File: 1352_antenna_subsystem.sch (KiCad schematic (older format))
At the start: 12 parts

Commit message: did more work on the schematic
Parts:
- AE1: renamed from AE; footprint (none) -> Connector_Coaxial:U.FL_Hirose_U.FL-R-SMT-1_Vertical
- C1, C2: renamed from C?; value C -> 1.1pF; footprint (none) -> Capacitor_SMD:C_0201_0603Metric_Pad0.64x0.40mm_HandSolder
- C3: renamed from C?; value C -> 12pF; footprint (none) -> Capacitor_SMD:C_0201_0603Metric_Pad0.64x0.40mm_HandSolder
- C4: renamed from C?; value C -> 1pF; footprint (none) -> Capacitor_SMD:C_0201_0603Metric_Pad0.64x0.40mm_HandSolder
- C5: renamed from C?; value C -> 47pF; footprint (none) -> Capacitor_SMD:C_0201_0603Metric_Pad0.64x0.40mm_HandSolder
- L1: renamed from L?; value L -> 15nH; footprint (none) -> Inductor_SMD:L_0201_0603Metric_Pad0.64x0.40mm_HandSolder
- L2, L3: renamed from L?; value L -> 2.4nH; footprint (none) -> Inductor_SMD:L_0201_0603Metric_Pad0.64x0.40mm_HandSolder
- L4: renamed from L?; value L -> 1nH; footprint (none) -> Inductor_SMD:L_0201_0603Metric_Pad0.64x0.40mm_HandSolder
- L5: renamed from L?; value L -> 3.3nH; footprint (none) -> Inductor_SMD:L_0201_0603Metric_Pad0.64x0.40mm_HandSolder
- gave numbers to parts that had none: 1
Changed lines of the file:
@@
 $EndDescr
 $Comp
-L power:GND #PWR?
+L power:GND #PWR0101
 U 1 1 603957EF
 P 3800 3950
-F 0 "#PWR?" H 3800 3700 50  0001 C CNN
+F 0 "#PWR0101" H 3800 3700 50  0001 C CNN
 F 1 "GND" H 3805 3777 50  0000 C CNN
 F 2 "" H 3800 3950 50  0001 C CNN
@@
 $EndComp
 $Comp
-L power:GND #PWR?
+L power:GND #PWR0102
 U 1 1 603965C6
 P 2250 4100
-F 0 "#PWR?" H 2250 3850 50  0001 C CNN
+F 0 "#PWR0102" H 2250 3850 50  0001 C CNN
 F 1 "GND" H 2255 3927 50  0000 C CNN
 F 2 "" H 2250 4100 50  0001 C CNN
@@
 $EndComp
 $Comp
-L Device:C C?
+L Device:C C1
 U 1 1 6039A1F9
 P 2250 3800
-F 0 "C?" H 2365 3846 50  0000 L CNN
-F 1 "C" H 2365 3755 50  0000 L CNN
-F 2 "" H 2288 3650 50  0001 C CNN
+F 0 "C1" H 2365 3846 50  0000 L CNN
+F 1 "1.1pF" H 2365 3755 50  0000 L CNN
+F 2 "Capacitor_SMD:C_0201_0603Metric_Pad0.64x0.40mm_HandSolder" H 2288 3650 50  0001 C CNN
 F 3 "~" H 2250 3800 50  0001 C CNN
 	1    2250 3800
@@
 $EndComp
 $Comp
-L Device:C C?
+L Device:C C5
 U 1 1 6039A7AD
 P 4650 3500
-F 0 "C?" V 4765 3546 50  0000 L CNN
-F 1 "C" V 4765 3455 50  0000 L CNN
-F 2 "" H 4688 3350 50  0001 C CNN
+F 0 "C5" V 4900 3450 50  0000 L CNN
+F 1 "47pF" V 4800 3400 50  0000 L CNN
+F 2 "Capacitor_SMD:C_0201_0603Metric_Pad0.64x0.40mm_HandSolder" H 4688 3350 50  0001 C CNN
 F 3 "~" H 4650 3500 50  0001 C CNN
 	1    4650 3500
@@
 $EndComp
 $Comp
-L Device:L L?
+L Device:L L2
 U 1 1 6039AD96
 P 2300 3200
-F 0 "L?" H 2353 3246 50  0000 L CNN
-F 1 "L" H 2353 3155 50  0000 L CNN
-F 2 "" H 2300 3200 50  0001 C CNN
+F 0 "L2" H 2150 3250 50  0000 L CNN
+F 1 "2.4nH" H 2050 3150 50  0000 L CNN
+F 2 "Inductor_SMD:L_0201_0603Metric_Pad0.64x0.40mm_HandSolder" H 2300 3200 50  0001 C CNN
 F 3 "~" H 2300 3200 50  0001 C CNN
 	1    2300 3200
@@
 $EndComp
 $Comp
-L Device:L L?
+L Device:L L3
 U 1 1 6039B183
 P 2550 3650
-F 0 "L?" V 2650 3650 50  0000 L CNN
-F 1 "L" V 2650 3600 50  0000 L CNN
-F 2 "" H 2550 3650 50  0001 C CNN
+F 0 "L3" V 2650 3550 50  0000 L CNN
+F 1 "2.4nH" V 2650 3650 50  0000 L CNN
+F 2 "Inductor_SMD:L_0201_0603Metric_Pad0.64x0.40mm_HandSolder" H 2550 3650 50  0001 C CNN
 F 3 "~" H 2550 3650 50  0001 C CNN
 	1    2550 3650
@@
 $EndComp
 $Comp
-L Device:L L?
+L Device:L L1
 U 1 1 6039B788
 P 2100 3500
-F 0 "L?" H 2153 3546 50  0000 L CNN
-F 1 "L" H 2153 3455 50  0000 L CNN
-F 2 "" H 2100 3500 50  0001 C CNN
+F 0 "L1" H 2000 3550 50  0000 L CNN
+F 1 "15nH" H 1900 3450 50  0000 L CNN
+F 2 "Inductor_SMD:L_0201_0603Metric_Pad0.64x0.40mm_HandSolder" H 2100 3500 50  0001 C CNN
 F 3 "~" H 2100 3500 50  0001 C CNN
 	1    2100 3500
@@
 	2100 3350 2300 3350
 $Comp
-L Device:C C?
+L Device:C C2
 U 1 1 603CD7B2
 P 2550 3350
-F 0 "C?" V 2298 3350 50  0000 C CNN
-F 1 "C" V 2389 3350 50  0000 C CNN
-F 2 "" H 2588 3200 50  0001 C CNN
+F 0 "C2" V 2600 3450 50  0000 C CNN
+F 1 "1.1pF" V 2500 3500 50  0000 C CNN
+F 2 "Capacitor_SMD:C_0201_0603Metric_Pad0.64x0.40mm_HandSolder" H 2588 3200 50  0001 C CNN
 F 3 "~" H 2550 3350 50  0001 C CNN
 	1    2550 3350
@@
 	3100 3500 3300 3500
 $Comp
-L Device:L L?
+L Device:L L4
 U 1 1 603CF711
 P 3450 3500
-F 0 "L?" V 3640 3500 50  0000 C CNN
-F 1 "L" V 3549 3500 50  0000 C CNN
-F 2 "" H 3450 3500 50  0001 C CNN
+F 0 "L4" V 3640 3500 50  0000 C CNN
+F 1 "1nH" V 3549 3500 50  0000 C CNN
+F 2 "Inductor_SMD:L_0201_0603Metric_Pad0.64x0.40mm_HandSolder" H 3450 3500 50  0001 C CNN
 F 3 "~" H 3450 3500 50  0001 C CNN
 	1    3450 3500
@@
 	2300 3050 2750 3050
 $Comp
-L power:GND #PWR?
+L power:GND #PWR0103
 U 1 1 603D2468
 P 3350 3050
-F 0 "#PWR?" H 3350 2800 50  0001 C CNN
+F 0 "#PWR0103" H 3350 2800 50  0001 C CNN
 F 1 "GND" V 3355 2922 50  0000 R CNN
 F 2 "" H 3350 3050 50  0001 C CNN
@@
 	3050 3050 3350 3050
 $Comp
-L Device:C C?
+L Device:C C3
 U 1 1 603D700A
 P 2900 3050
-F 0 "C?" V 2648 3050 50  0000 C CNN
-F 1 "C" V 2739 3050 50  0000 C CNN
-F 2 "" H 2938 2900 50  0001 C CNN
+F 0 "C3" V 2648 3050 50  0000 C CNN
+F 1 "12pF" V 2739 3050 50  0000 C CNN
+F 2 "Capacitor_SMD:C_0201_0603Metric_Pad0.64x0.40mm_HandSolder" H 2938 2900 50  0001 C CNN
 F 3 "~" H 2900 3050 50  0001 C CNN
 	1    2900 3050
@@
 $EndComp
 $Comp
-L Device:L L?
+L Device:L L5
 U 1 1 603D983C
 P 4150 3500
-F 0 "L?" V 4340 3500 50  0000 C CNN
-F 1 "L" V 4249 3500 50  0000 C CNN
-F 2 "" H 4150 3500 50  0001 C CNN
+F 0 "L5" V 4340 3500 50  0000 C CNN
+F 1 "3.3nH" V 4249 3500 50  0000 C CNN
+F 2 "Inductor_SMD:L_0201_0603Metric_Pad0.64x0.40mm_HandSolder" H 4150 3500 50  0001 C CNN
 F 3 "~" H 4150 3500 50  0001 C CNN
 	1    4150 3500
@@
 $EndComp
 $Comp
-L Device:C C?
+L Device:C C4
 U 1 1 603DBF1C
 P 3800 3650
-F 0 "C?" H 3915 3696 50  0000 L CNN
-F 1 "C" H 3915 3605 50  0000 L CNN
-F 2 "" H 3838 3500 50  0001 C CNN
+F 0 "C4" H 3915 3696 50  0000 L CNN
+F 1 "1pF" H 3915 3605 50  0000 L CNN
+F 2 "Capacitor_SMD:C_0201_0603Metric_Pad0.64x0.40mm_HandSolder" H 3838 3500 50  0001 C CNN
 F 3 "~" H 3800 3650 50  0001 C CNN
 	1    3800 3650
@@
 	5300 3500 5300 3300
 $Comp
-L Device:Antenna AE
+L Device:Antenna AE1
 U 1 1 603E2167
 P 5300 3100
-F 0 "AE" H 5380 3089 50  0000 L CNN
+F 0 "AE1" H 5380 3089 50  0000 L CNN
 F 1 "50Ω" H 5380 2998 50  0000 L CNN
-F 2 "" H 5300 3100 50  0001 C CNN
+F 2 "Connector_Coaxial:U.FL_Hirose_U.FL-R-SMT-1_Vertical" H 5300 3100 50  0001 C CNN
 F 3 "~" H 5300 3100 50  0001 C CNN
 	1    5300 3100
@@
 $EndComp
 $Comp
-L cc1352:cc1352p U?
+L cc1352:cc1352p U1
 U 1 1 603F4DE1
 P 1050 4800
-F 0 "U?" H 2209 4054 50  0001 C BNN
+F 0 "U1" H 2209 4054 50  0001 C BNN
 F 1 "cc1352p" H 2050 3850 50  0000 R CNN
 F 2 "Package_DFN_QFN:VQFN-48-1EP_7x7mm_P0.5mm_EP5.15x5.15mm" H 2400 3750 20  0000 R CNN

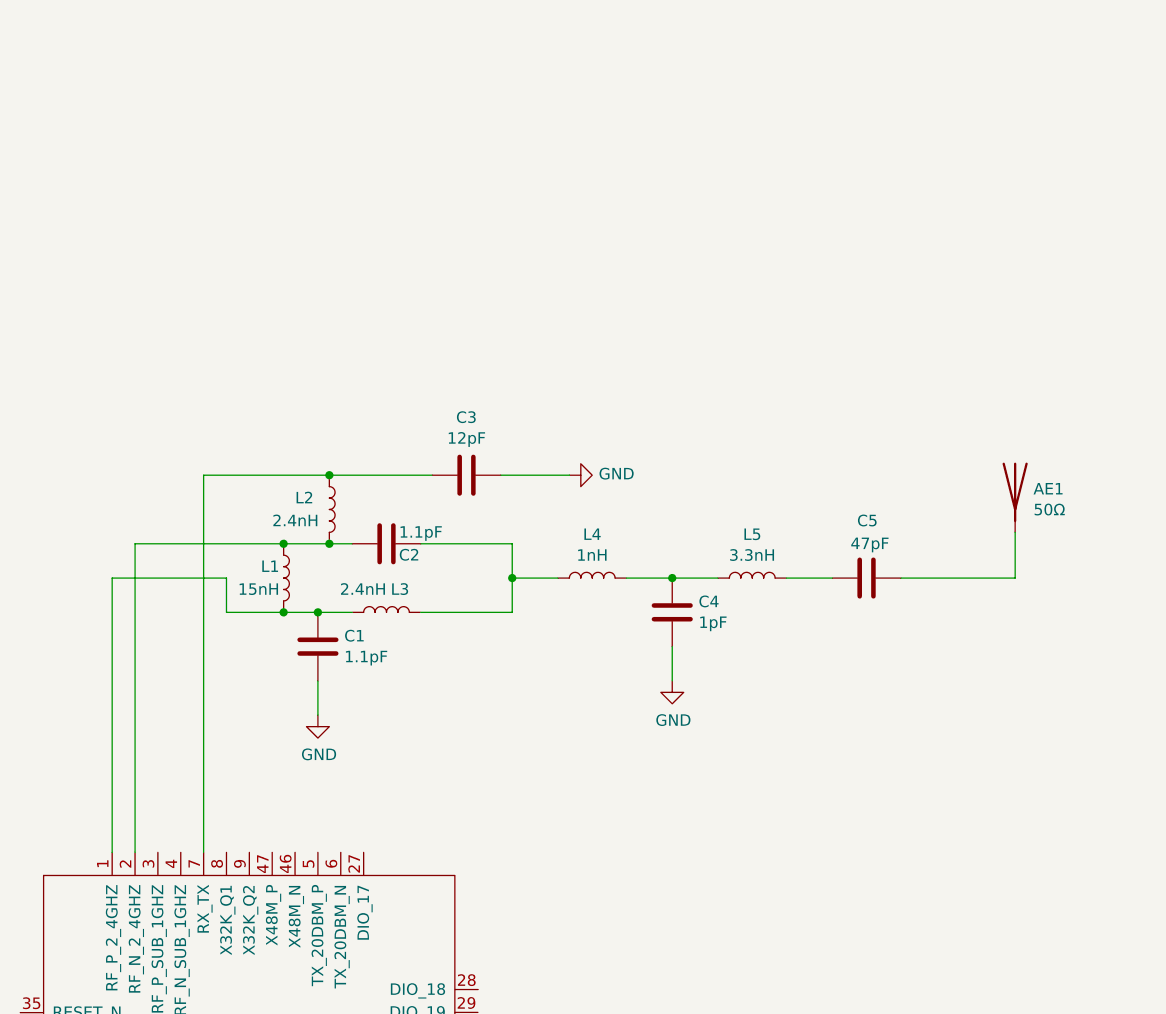
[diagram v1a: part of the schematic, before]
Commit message: Finished schematic and PCB design for 2.4GHz and Sub 1GHz
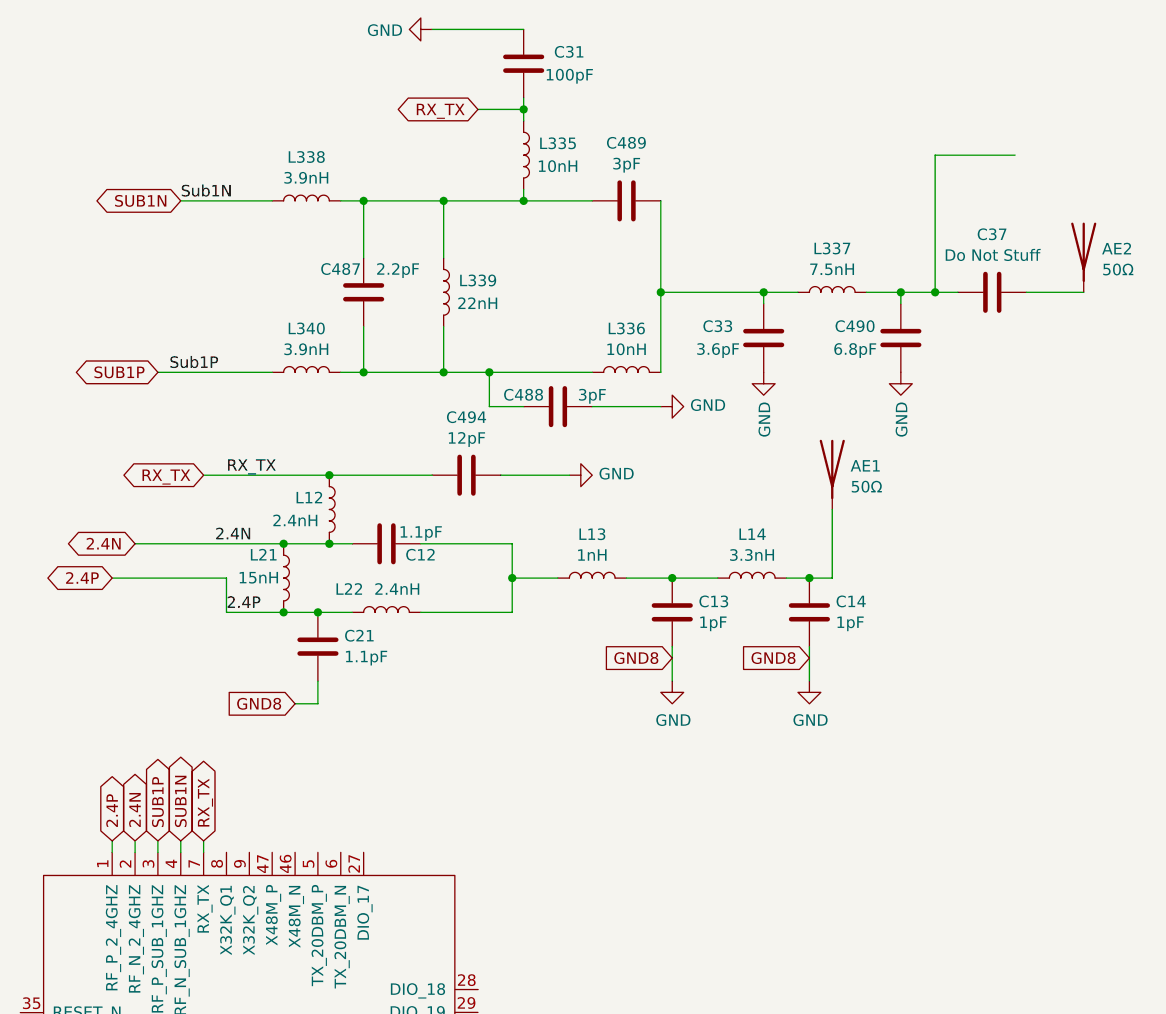
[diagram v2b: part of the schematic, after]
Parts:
- removed C5: 47pF, Capacitor_SMD:C_0201_0603Metric_Pad0.64x0.40mm_HandSolder, symbol Device:C
- added AE2: 50Ω, Connector_Coaxial:U.FL_Hirose_U.FL-R-SMT-1_Vertical, symbol Device:Antenna
- added C14: 1pF, Capacitor_SMD:C_0805_2012Metric_Pad1.18x1.45mm_HandSolder, symbol Device:C
- added C31: 100pF, Capacitor_SMD:C_0805_2012Metric_Pad1.18x1.45mm_HandSolder, symbol Device:C
- added C33: 3.6pF, Capacitor_SMD:C_0805_2012Metric_Pad1.18x1.45mm_HandSolder, symbol Device:C
- added C37: Do Not Stuff, Capacitor_SMD:C_0805_2012Metric_Pad1.18x1.45mm_HandSolder, symbol Device:C
- added C487: 2.2pF, Capacitor_SMD:C_0805_2012Metric_Pad1.18x1.45mm_HandSolder, symbol Device:C
- added C488, C489: 3pF, Capacitor_SMD:C_0805_2012Metric_Pad1.18x1.45mm_HandSolder, symbol Device:C
- added C490: 6.8pF, Capacitor_SMD:C_0805_2012Metric_Pad1.18x1.45mm_HandSolder, symbol Device:C
- added L335, L336: 10nH, Inductor_SMD:L_0805_2012Metric_Pad1.15x1.40mm_HandSolder, symbol Device:L
- added L337: 7.5nH, Inductor_SMD:L_0805_2012Metric_Pad1.15x1.40mm_HandSolder, symbol Device:L
- added L338, L340: 3.9nH, Inductor_SMD:L_0805_2012Metric_Pad1.15x1.40mm_HandSolder, symbol Device:L
- added L339: 22nH, Inductor_SMD:L_0805_2012Metric_Pad1.15x1.40mm_HandSolder, symbol Device:L
- C12: renamed from C2; footprint Capacitor_SMD:C_0201_0603Metric_Pad0.64x0.40mm_HandSolder -> Capacitor_SMD:C_0805_2012Metric_Pad1.18x1.45mm_HandSolder
- C13: renamed from C4; footprint Capacitor_SMD:C_0201_0603Metric_Pad0.64x0.40mm_HandSolder -> Capacitor_SMD:C_0805_2012Metric_Pad1.18x1.45mm_HandSolder
- C21: renamed from C1; footprint Capacitor_SMD:C_0201_0603Metric_Pad0.64x0.40mm_HandSolder -> Capacitor_SMD:C_0805_2012Metric_Pad1.18x1.45mm_HandSolder
- C494: renamed from C3; footprint Capacitor_SMD:C_0201_0603Metric_Pad0.64x0.40mm_HandSolder -> Capacitor_SMD:C_0805_2012Metric_Pad1.18x1.45mm_HandSolder
- L12: renamed from L2; footprint Inductor_SMD:L_0201_0603Metric_Pad0.64x0.40mm_HandSolder -> Inductor_SMD:L_0805_2012Metric_Pad1.15x1.40mm_HandSolder
- L13: renamed from L4; footprint Inductor_SMD:L_0201_0603Metric_Pad0.64x0.40mm_HandSolder -> Inductor_SMD:L_0805_2012Metric_Pad1.15x1.40mm_HandSolder
- L14: renamed from L5; footprint Inductor_SMD:L_0201_0603Metric_Pad0.64x0.40mm_HandSolder -> Inductor_SMD:L_0805_2012Metric_Pad1.15x1.40mm_HandSolder
- L21: renamed from L1; footprint Inductor_SMD:L_0201_0603Metric_Pad0.64x0.40mm_HandSolder -> Inductor_SMD:L_0805_2012Metric_Pad1.15x1.40mm_HandSolder
- L22: renamed from L3; footprint Inductor_SMD:L_0201_0603Metric_Pad0.64x0.40mm_HandSolder -> Inductor_SMD:L_0805_2012Metric_Pad1.15x1.40mm_HandSolder
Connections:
- net GND: now also C14.2, C31.2, C33.2, C488.1, C490.2
- net 2.4P: now reaches C21.1, L21.2, L22.1, U1.1 (RF_P_2_4GHZ)
- net at L14.2: now also AE1.1 (A), C14.1
- net RX_TX: now reaches C494.2, L12.1, U1.7 (RX_TX)
- net RX_TX: now also C31.1, L335.1
- net 2.4N: now reaches C12.2, L12.2, L21.1, U1.2 (RF_N_2_4GHZ)
- net SUB1P: now reaches U1.3 (RF_P_SUB_1GHZ)
- net SUB1P: now also L340.1
- net SUB1N: now reaches U1.4 (RF_N_SUB_1GHZ)
- net SUB1N: now also L338.1
- new net: C487.1, C489.2, L335.2, L338.2, L339.1
- new net: C487.2, C488.2, L336.1, L339.2, L340.2
- new net: C33.1, C489.1, L336.2, L337.1
- new net: C37.2, C490.1, L337.2
- new net: AE2.1 (A), C37.1
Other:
- moved on the sheet: AE1
